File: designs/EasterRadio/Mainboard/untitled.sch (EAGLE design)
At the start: 50 parts, among them IC1 74HC595D, IC2 74HC595D, IC3 74HC595D, IC4 Analog Digital

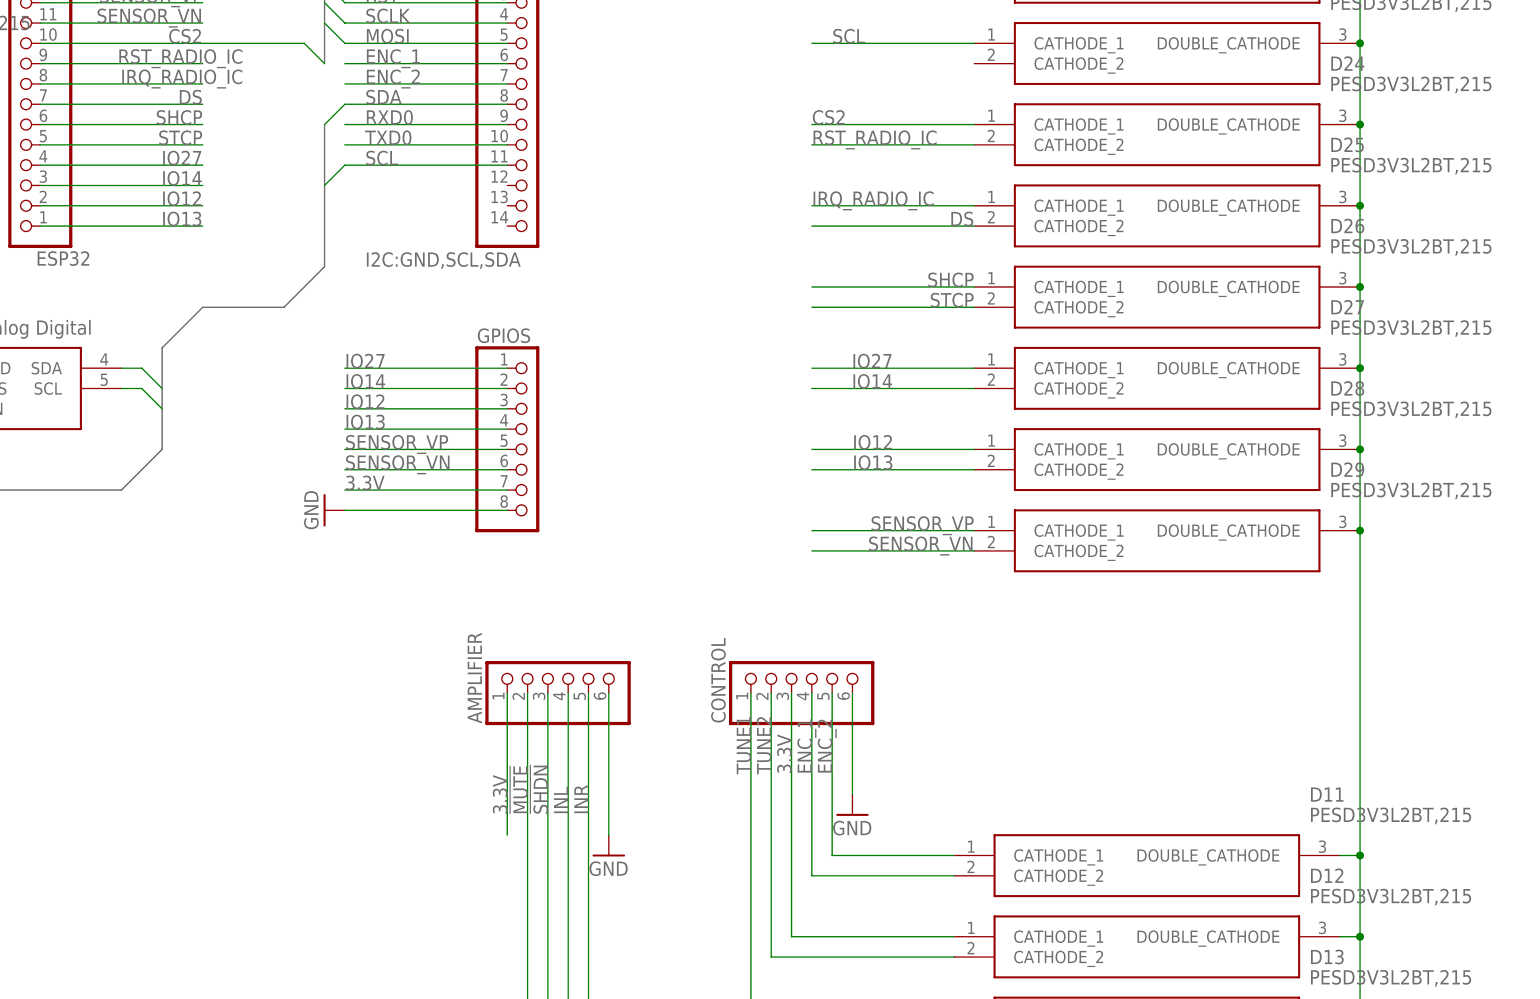
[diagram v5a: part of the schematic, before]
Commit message: changed poti and encoder pcb to correct schematic and brd + mainboard change for push btn on rotary encoder
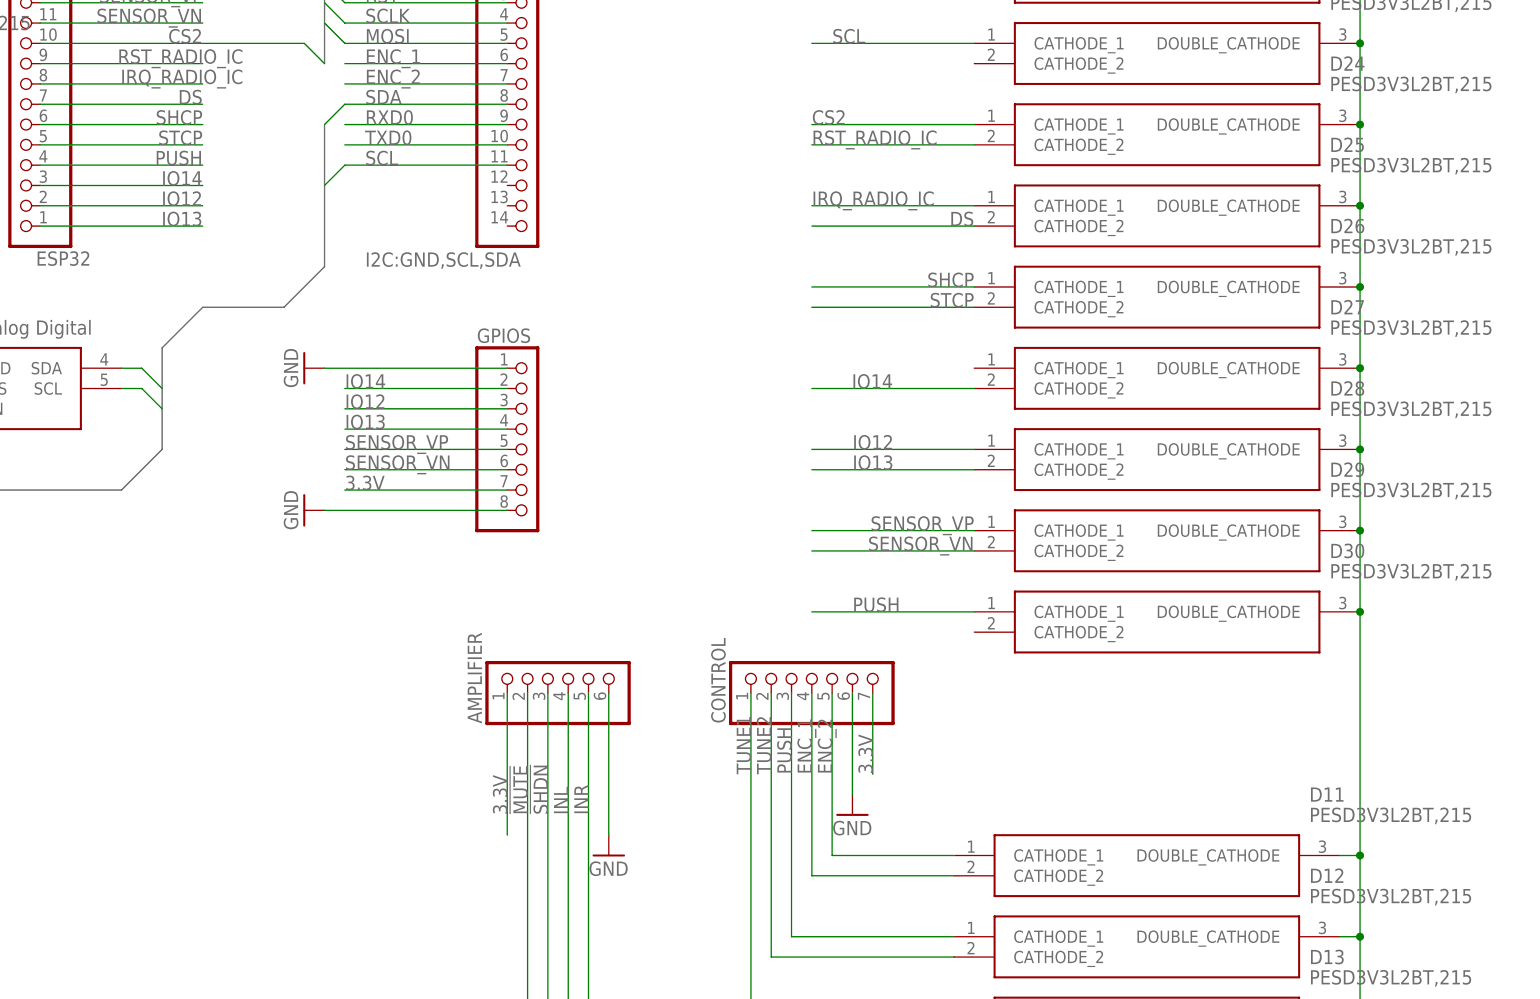
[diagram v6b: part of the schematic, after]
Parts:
- added D30: PESD3V3L2BT,215, MouserUseful:PESD3V3L2BT,215
- CONTROL: device pinhead:PINHD-1X6 -> pinhead:PINHD-1X7
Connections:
- removed net IO27: D27.CATHODE_1, ESP32.4, GPIOS.1
- new net PUSH: CONTROL.3, D12.CATHODE_1, D30.CATHODE_1, ESP32.4
- net 3.3V: now also CONTROL.7; no longer CONTROL.3, D12.CATHODE_1
- net GND: now also D30.DOUBLE_CATHODE, GPIOS.1
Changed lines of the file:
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@@
 <part name="ESP32" library="pinhead" library_urn="urn:adsk.eagle:library:325" deviceset="PINHD-1X14" device="" package3d_urn="urn:adsk.eagle:package:22417/2"/>
 <part name="AMPLIFIER" library="pinhead" library_urn="urn:adsk.eagle:library:325" deviceset="PINHD-1X6" device="" package3d_urn="urn:adsk.eagle:package:22472/2"/>
-<part name="CONTROL" library="pinhead" library_urn="urn:adsk.eagle:library:325" deviceset="PINHD-1X6" device="" package3d_urn="urn:adsk.eagle:package:22472/2"/>
 <part name="DISPLAY" library="pinhead" library_urn="urn:adsk.eagle:library:325" deviceset="PINHD-1X8" device="" package3d_urn="urn:adsk.eagle:package:22409/2"/>
 <part name="PROG" library="pinhead" library_urn="urn:adsk.eagle:library:325" deviceset="PINHD-1X4" device="" package3d_urn="urn:adsk.eagle:package:22407/2"/>
@@
 <part name="GPIOS" library="pinhead" library_urn="urn:adsk.eagle:library:325" deviceset="PINHD-1X8" device="" package3d_urn="urn:adsk.eagle:package:22409/2"/>
 <part name="GND15" library="supply1" library_urn="urn:adsk.eagle:library:371" deviceset="GND" device=""/>
+<part name="CONTROL" library="pinhead" library_urn="urn:adsk.eagle:library:325" deviceset="PINHD-1X7" device="" package3d_urn="urn:adsk.eagle:package:22477/2"/>
+<part name="GND19" library="supply1" library_urn="urn:adsk.eagle:library:371" deviceset="GND" device=""/>
+<part name="D30" library="MouserUseful" deviceset="PESD3V3L2BT,215" device=""/>
 </parts>
 <sheets>
@@
 <attribute name="VALUE" x="256.54" y="80.01" size="1.778" layer="96" rot="R90"/>
 </instance>
-<instance part="CONTROL" gate="A" x="276.86" y="86.36" smashed="yes" rot="R90">
-<attribute name="NAME" x="266.065" y="80.01" size="1.778" layer="95" rot="R90"/>
-<attribute name="VALUE" x="287.02" y="80.01" size="1.778" layer="96" rot="R90"/>
-</instance>
 <instance part="DISPLAY" gate="A" x="124.46" y="185.42" smashed="yes" rot="R180">
 <attribute name="NAME" x="130.81" y="172.085" size="1.778" layer="95" rot="R180"/>
@@
 <attribute name="VALUE" x="234.95" y="101.6" size="1.778" layer="96"/>
 </instance>
-<instance part="GND15" gate="1" x="215.9" y="106.68" smashed="yes" rot="R270">
-<attribute name="VALUE" x="213.36" y="109.22" size="1.778" layer="96" rot="R270"/>
+<instance part="GND15" gate="1" x="213.36" y="106.68" smashed="yes" rot="R270">
+<attribute name="VALUE" x="210.82" y="109.22" size="1.778" layer="96" rot="R270"/>
+</instance>
+<instance part="CONTROL" gate="A" x="276.86" y="86.36" smashed="yes" rot="R90">
+<attribute name="NAME" x="266.065" y="80.01" size="1.778" layer="95" rot="R90"/>
+<attribute name="VALUE" x="289.56" y="80.01" size="1.778" layer="96" rot="R90"/>
+</instance>
+<instance part="GND19" gate="1" x="213.36" y="124.46" smashed="yes" rot="R270">
+<attribute name="VALUE" x="210.82" y="127" size="1.778" layer="96" rot="R270"/>
+</instance>
+<instance part="D30" gate="G$1" x="297.18" y="93.98" smashed="yes">
+<attribute name="NAME" x="341.63" y="101.6" size="1.778" layer="95" align="center-left"/>
+<attribute name="VALUE" x="341.63" y="99.06" size="1.778" layer="96" align="center-left"/>
 </instance>
 </instances>
@@
 <label x="73.66" y="48.26" size="1.778" layer="95" rot="R90" align="bottom-right"/>
 <pinref part="RADIO_IC" gate="A" pin="10"/>
-</segment>
-<segment>
-<pinref part="CONTROL" gate="A" pin="3"/>
-<label x="274.32" y="73.66" size="1.778" layer="95" rot="R90"/>
-<wire x1="274.32" y1="83.82" x2="274.32" y2="53.34" width="0.1524" layer="91"/>
-<pinref part="D12" gate="G$1" pin="CATHODE_1"/>
-<wire x1="274.32" y1="53.34" x2="294.64" y2="53.34" width="0.1524" layer="91"/>
 </segment>
 <segment>
@@
 <wire x1="238.76" y1="109.22" x2="218.44" y2="109.22" width="0.1524" layer="91"/>
 <label x="218.44" y="109.22" size="1.778" layer="95"/>
+</segment>
+<segment>
+<pinref part="CONTROL" gate="A" pin="7"/>
+<wire x1="284.48" y1="83.82" x2="284.48" y2="73.66" width="0.1524" layer="91"/>
+<label x="284.48" y="73.66" size="1.778" layer="95" rot="R90"/>
 </segment>
 </net>
@@
 </segment>
 <segment>
-<pinref part="CONTROL" gate="A" pin="6"/>
 <wire x1="281.94" y1="83.82" x2="281.94" y2="71.12" width="0.1524" layer="91"/>
 <pinref part="GND8" gate="1" pin="GND"/>
+<pinref part="CONTROL" gate="A" pin="6"/>
 </segment>
 <segment>
@@
 <wire x1="345.44" y1="205.74" x2="345.44" y2="215.9" width="0.1524" layer="91"/>
 <junction x="345.44" y="205.74"/>
-<wire x1="345.44" y1="104.14" x2="345.44" y2="63.5" width="0.1524" layer="91"/>
+<wire x1="345.44" y1="104.14" x2="345.44" y2="93.98" width="0.1524" layer="91"/>
 <junction x="345.44" y="104.14"/>
 <junction x="345.44" y="63.5"/>
 <pinref part="D16" gate="G$1" pin="DOUBLE_CATHODE"/>
 <pinref part="D17" gate="G$1" pin="DOUBLE_CATHODE"/>
+<wire x1="345.44" y1="93.98" x2="345.44" y2="63.5" width="0.1524" layer="91"/>
 <wire x1="345.44" y1="269.24" x2="345.44" y2="259.08" width="0.1524" layer="91"/>
 <wire x1="345.44" y1="259.08" x2="345.44" y2="215.9" width="0.1524" layer="91"/>
 <junction x="345.44" y="259.08"/>
 <junction x="345.44" y="215.9"/>
+<pinref part="D30" gate="G$1" pin="DOUBLE_CATHODE"/>
+<junction x="345.44" y="93.98"/>
 </segment>
 <segment>
@@
 <segment>
 <pinref part="GPIOS" gate="A" pin="8"/>
-<wire x1="238.76" y1="106.68" x2="218.44" y2="106.68" width="0.1524" layer="91"/>
+<wire x1="238.76" y1="106.68" x2="215.9" y2="106.68" width="0.1524" layer="91"/>
 <pinref part="GND15" gate="1" pin="GND"/>
+</segment>
+<segment>
+<wire x1="238.76" y1="124.46" x2="215.9" y2="124.46" width="0.1524" layer="91"/>
+<pinref part="GPIOS" gate="A" pin="1"/>
+<pinref part="GND19" gate="1" pin="GND"/>
 </segment>
 </net>
@@
 </segment>
 </net>
-<net name="IO27" class="0">
-<segment>
-<pinref part="ESP32" gate="A" pin="4"/>
-<wire x1="180.34" y1="149.86" x2="200.66" y2="149.86" width="0.1524" layer="91"/>
-<label x="200.66" y="149.86" size="1.778" layer="95" align="bottom-right"/>
-</segment>
-<segment>
-<wire x1="238.76" y1="124.46" x2="218.44" y2="124.46" width="0.1524" layer="91"/>
-<label x="218.44" y="124.46" size="1.778" layer="95" rot="R180" align="top-right"/>
-<pinref part="GPIOS" gate="A" pin="1"/>
-</segment>
-<segment>
-<wire x1="276.86" y1="124.46" x2="297.18" y2="124.46" width="0.1524" layer="91"/>
-<label x="287.02" y="124.46" size="1.778" layer="95" align="bottom-right"/>
-<pinref part="D27" gate="G$1" pin="CATHODE_1"/>
-</segment>
-</net>
 <net name="CS2" class="0">
 <segment>
@@
 </segment>
 <segment>
-<pinref part="CONTROL" gate="A" pin="4"/>
 <wire x1="276.86" y1="83.82" x2="276.86" y2="60.96" width="0.1524" layer="91"/>
 <label x="276.86" y="73.66" size="1.778" layer="95" rot="R90"/>
 <pinref part="D11" gate="G$1" pin="CATHODE_2"/>
 <wire x1="276.86" y1="60.96" x2="294.64" y2="60.96" width="0.1524" layer="91"/>
+<pinref part="CONTROL" gate="A" pin="4"/>
 </segment>
 </net>
@@
 </segment>
 <segment>
-<pinref part="CONTROL" gate="A" pin="5"/>
 <wire x1="279.4" y1="83.82" x2="279.4" y2="63.5" width="0.1524" layer="91"/>
 <label x="279.4" y="73.66" size="1.778" layer="95" rot="R90"/>
 <pinref part="D11" gate="G$1" pin="CATHODE_1"/>
 <wire x1="279.4" y1="63.5" x2="294.64" y2="63.5" width="0.1524" layer="91"/>
+<pinref part="CONTROL" gate="A" pin="5"/>
 </segment>
 </net>
@@
 </segment>
 <segment>
-<pinref part="CONTROL" gate="A" pin="1"/>
 <label x="269.24" y="73.66" size="1.778" layer="95" rot="R90"/>
 <wire x1="269.24" y1="83.82" x2="269.24" y2="43.18" width="0.1524" layer="91"/>
 <pinref part="D13" gate="G$1" pin="CATHODE_1"/>
 <wire x1="269.24" y1="43.18" x2="294.64" y2="43.18" width="0.1524" layer="91"/>
+<pinref part="CONTROL" gate="A" pin="1"/>
 </segment>
 </net>
@@
 </segment>
 <segment>
-<pinref part="CONTROL" gate="A" pin="2"/>
 <label x="271.78" y="73.66" size="1.778" layer="95" rot="R90"/>
 <wire x1="271.78" y1="83.82" x2="271.78" y2="50.8" width="0.1524" layer="91"/>
 <pinref part="D12" gate="G$1" pin="CATHODE_2"/>
 <wire x1="271.78" y1="50.8" x2="294.64" y2="50.8" width="0.1524" layer="91"/>
+<pinref part="CONTROL" gate="A" pin="2"/>
 </segment>
 </net>
@@
 </segment>
 </net>
+<net name="PUSH" class="0">
+<segment>
+<pinref part="CONTROL" gate="A" pin="3"/>
+<label x="274.32" y="73.66" size="1.778" layer="95" rot="R90"/>
+<wire x1="274.32" y1="83.82" x2="274.32" y2="53.34" width="0.1524" layer="91"/>
+<pinref part="D12" gate="G$1" pin="CATHODE_1"/>
+<wire x1="274.32" y1="53.34" x2="294.64" y2="53.34" width="0.1524" layer="91"/>
+</segment>
+<segment>
+<pinref part="ESP32" gate="A" pin="4"/>
+<wire x1="180.34" y1="149.86" x2="200.66" y2="149.86" width="0.1524" layer="91"/>
+<label x="200.66" y="149.86" size="1.778" layer="95" align="bottom-right"/>
+</segment>
+<segment>
+<pinref part="D30" gate="G$1" pin="CATHODE_1"/>
+<wire x1="297.18" y1="93.98" x2="276.86" y2="93.98" width="0.1524" layer="91"/>
+<label x="281.94" y="93.98" size="1.778" layer="95"/>
+</segment>
+</net>
